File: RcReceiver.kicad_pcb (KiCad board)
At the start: 2 copper layers, 0 parts

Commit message: Add some footprints
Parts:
- added A1: E28-2G4M20S, miscellaneous:E28-2G4M20S, F.Cu at (53.0, 76.8)
- added A2: E28-2G4M20S, miscellaneous:E28-2G4M20S, F.Cu at (70.7, 76.8)
- added C1: 100nF, Capacitor_SMD:C_0402_1005Metric, F.Cu at (105.9, 83.2)
- added C10: 1uF, Capacitor_SMD:C_0402_1005Metric, F.Cu at (107.8, 82.2)
- added C11: 12pF, Capacitor_SMD:C_0402_1005Metric, F.Cu at (107.8, 83.2)
- added C12: 12pF, Capacitor_SMD:C_0402_1005Metric, F.Cu at (109.8, 83.2)
- added C13: 10uF, Capacitor_Tantalum_SMD:CP_EIA-3216-18_Kemet-A, F.Cu at (57.9, 103.3)
- added C14: 1uF, Capacitor_SMD:C_0402_1005Metric, F.Cu at (45.0, 105.9)
- added C15: 1uF, Capacitor_SMD:C_0402_1005Metric, F.Cu at (53.5, 103.8)
- added C16: 10uF, Capacitor_Tantalum_SMD:CP_EIA-3216-18_Kemet-A, F.Cu at (46.4, 104.4)
- added C17: 470pF, Capacitor_SMD:C_0402_1005Metric, F.Cu at (54.6, 105.8)
- added C18: 100nF, Capacitor_SMD:C_0402_1005Metric, F.Cu at (58.4, 104.8)
- added C19: 100nF, Capacitor_SMD:C_0402_1005Metric, F.Cu at (54.6, 104.8)
- added C2: 100nF, Capacitor_SMD:C_0402_1005Metric, F.Cu at (108.1, 81.2)
- added C20: 470pF, Capacitor_SMD:C_0402_1005Metric, F.Cu at (52.7, 105.8)
- added C21: 470pF, Capacitor_SMD:C_0402_1005Metric, F.Cu at (52.7, 104.8)
- added C22: 100nF, Capacitor_SMD:C_0402_1005Metric, F.Cu at (49.7, 103.8)
- added C23: 470pF, Capacitor_SMD:C_0402_1005Metric, F.Cu at (50.8, 105.8)
- added C24: 470pF, Capacitor_SMD:C_0402_1005Metric, F.Cu at (48.8, 105.9)
- added C25: 470pF, Capacitor_SMD:C_0402_1005Metric, F.Cu at (51.6, 103.8)
- added C26: 470pF, Capacitor_SMD:C_0402_1005Metric, F.Cu at (46.9, 105.9)
- added C27: 470pF, Capacitor_SMD:C_0402_1005Metric, F.Cu at (49.7, 104.8)
- added C28: 100nF, Capacitor_SMD:C_0402_1005Metric, F.Cu at (48.8, 91.1)
- added C29: 1uF, Capacitor_SMD:C_0402_1005Metric, F.Cu at (45.0, 91.1)
- added C3: 100nF, Capacitor_SMD:C_0402_1005Metric, F.Cu at (110.0, 81.2)
- added C30: 1uF, Capacitor_SMD:C_0402_1005Metric, F.Cu at (88.9, 63.4)
- added C31: 10uF, Capacitor_Tantalum_SMD:CP_EIA-3216-18_Kemet-A, F.Cu at (81.8, 63.9)
- added C32: 100nF, Capacitor_SMD:C_0402_1005Metric, F.Cu at (46.9, 91.1)
- added C4: 100nF, Capacitor_SMD:C_0402_1005Metric, F.Cu at (111.9, 81.2)
- added C5: 100nF, Capacitor_SMD:C_0402_1005Metric, F.Cu at (113.8, 81.2)
- added C6: 4.7uF, Capacitor_SMD:C_0402_1005Metric, F.Cu at (105.9, 82.2)
- added C7: 1uF, Capacitor_SMD:C_0402_1005Metric, F.Cu at (109.8, 82.2)
- added C8: 1uF, Capacitor_SMD:C_0402_1005Metric, F.Cu at (111.7, 82.2)
- added C9: 10nF, Capacitor_SMD:C_0402_1005Metric, F.Cu at (113.6, 82.2)
- added D1: LED, LED_SMD:LED_0402_1005Metric, F.Cu at (106.2, 81.2)
- added FB1: Ferrite_Bead, Inductor_SMD:L_0402_1005Metric, F.Cu at (131.8, 73.9)
- added J1: VBAT, Connector_PinHeader_1.27mm:PinHeader_1x02_P1.27mm_Vertical, F.Cu at (100.0, 81.9)
- added J13: CAN, Connector_JST:JST_PH_B3B-PH-SM4-TB_1x03-1MP_P2.00mm_Vertical, F.Cu at (49.8, 99.5)
- added J2: SWD, Connector_JST:JST_SH_BM05B-SRSS-TB_1x05-1MP_P1.00mm_Vertical, F.Cu at (131.5, 65.5)
- added J3: I2C, Connector_JST:JST_SH_BM05B-SRSS-TB_1x05-1MP_P1.00mm_Vertical, F.Cu at (120.7, 76.0)
- added J4: USART1, Connector_JST:JST_SH_BM04B-SRSS-TB_1x04-1MP_P1.00mm_Vertical, F.Cu at (120.2, 81.2)
- added J5: Analog input, Connector_JST:JST_SH_BM05B-SRSS-TB_1x05-1MP_P1.00mm_Vertical, F.Cu at (130.5, 70.7)
- added J6: GPS, Connector_JST:JST_SH_BM06B-SRSS-TB_1x06-1MP_P1.00mm_Vertical, F.Cu at (121.2, 70.7)
- added J7: SPI3, Connector_JST:JST_SH_BM07B-SRSS-TB_1x07-1MP_P1.00mm_Vertical, F.Cu at (121.7, 65.5)
- added R1: 2k2, Resistor_SMD:R_0402_1005Metric, F.Cu at (129.9, 74.9)
- added R2: 470k, Resistor_SMD:R_0402_1005Metric, F.Cu at (125.0, 79.1)
- added R3: 10k, Resistor_SMD:R_0402_1005Metric, F.Cu at (126.0, 77.6)
- added R4: 1k, Resistor_SMD:R_0402_1005Metric, F.Cu at (129.9, 73.9)
- added R5: 1k, Resistor_SMD:R_0402_1005Metric, F.Cu at (113.6, 83.2)
- added R6: 1k, Resistor_SMD:R_0402_1005Metric, F.Cu at (111.7, 83.2)
- added R7: 470k, Resistor_SMD:R_0402_1005Metric, F.Cu at (56.5, 106.4)
- added R8: 4k7, Resistor_SMD:R_0402_1005Metric, F.Cu at (56.5, 104.8)
- added R9: 120R, Resistor_SMD:R_0402_1005Metric, F.Cu at (61.9, 99.8)
- added U1: LP38693-3.3, miscellaneous:WSON-6_3x3mm_Pitch0.95mm, F.Cu at (127.0, 75.2)
- added U2: STM32L476VGT6, Package_QFP:LQFP-100_14x14mm_P0.5mm, F.Cu at (107.3, 71.8)
- added U3: LP38693-5.0, miscellaneous:WSON-6_3x3mm_Pitch0.95mm, F.Cu at (62.1, 104.1)
- added U4: TXB0108DQSR, Package_SON:USON-20_2x4mm_P0.4mm, F.Cu at (62.6, 97.0)
- added U5: MCP2551, digikey-footprints:SOIC-8_W3.9mm, F.Cu at (58.2, 98.5)
- added U6: LP38693SD-3.3, miscellaneous:WSON-6_3x3mm_Pitch0.95mm, F.Cu at (86.0, 64.7)
- added Y1: 16MHz, Oscillator:Oscillator_SMD_SeikoEpson_SG210-4Pin_2.5x2.0mm, F.Cu at (103.3, 82.1)

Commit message: Create PCB
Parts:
- added D2: LED_ARGB, miscellaneous:LED_Lumex-LX0404, F.Cu at (162.5, 60.0)
- added J10: Servo3, miscellaneous:PinHeader_1x03_P1.27mm_Side, F.Cu at (186.0, 52.4)
- added J11: Servo4, miscellaneous:PinHeader_1x03_P1.27mm_Side, F.Cu at (186.0, 54.9)
- added J12: Servo5, miscellaneous:PinHeader_1x03_P1.27mm_Side, F.Cu at (186.0, 57.4)
- added J14: Servo6, miscellaneous:PinHeader_1x03_P1.27mm_Side, F.Cu at (186.0, 62.5)
- added J15: Servo7, miscellaneous:PinHeader_1x03_P1.27mm_Side, F.Cu at (186.0, 65.0)
- added J16: Servo8, miscellaneous:PinHeader_1x03_P1.27mm_Side, F.Cu at (186.0, 67.6)
- added J8: Servo1, miscellaneous:PinHeader_1x03_P1.27mm_Side, F.Cu at (186.0, 47.3)
- added J9: Servo2, miscellaneous:PinHeader_1x03_P1.27mm_Side, F.Cu at (186.0, 49.8)
- A1, A2, J2, J3, J7: moved to B.Cu
- R5, R6: value 1k -> 470
- moved C24 138.3 mm to (169.5, 38.4)
- moved R7 135.0 mm to (181.6, 55.5), turned to 90 degrees
- moved C27 133.5 mm to (168.2, 43.5)
- moved C14 132.6 mm to (158.7, 37.7)
- moved C15 126.0 mm to (163.1, 41.6)
- moved U4 121.7 mm to (177.7, 57.4)
- moved C19 120.7 mm to (172.7, 79.7)
- moved A1 120.1 mm to (172.0, 60.6), turned to 180 degrees
- moved C25 120.0 mm to (170.8, 89.2)
- moved C26 119.3 mm to (165.0, 89.2)
- moved U3 118.3 mm to (179.0, 86.1)
- moved C17 112.9 mm to (164.4, 79.7)
- moved R9 111.9 mm to (172.7, 83.5)
- moved C22 110.6 mm to (159.3, 89.2)
- moved C21 109.6 mm to (159.3, 79.7)
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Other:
- board outline added: 50 x 29.5 mm

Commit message: Place all the components on the board
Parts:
- added C33: 100nF, Capacitor_SMD:C_0402_1005Metric, F.Cu at (143.8, 47.9)
- added J17: GND for the Servo connectors, Connector_PinHeader_2.54mm:PinHeader_1x01_P2.54mm_Vertical, B.Cu at (184.1, 68.9)
- added REF**: KiCad-Logo2_6mm_SilkScreen, Symbol:KiCad-Logo2_6mm_SilkScreen, F.Cu at (176.1, 72.1)
- added REF**: OSHW-Logo2_7.3x6mm_SilkScreen, Symbol:OSHW-Logo2_7.3x6mm_SilkScreen, F.Cu at (167.8, 49.6)
- C28, C32: moved to B.Cu
- J13: footprint Connector_JST:JST_PH_B3B-PH-SM4-TB_1x03-1MP_P2.00mm_Vertical -> Connector_JST:JST_SH_BM03B-SRSS-TB_1x03-1MP_P1.00mm_Vertical
- moved C7 52.4 mm to (174.3, 63.2)
- moved C32 45.4 mm to (181.6, 50.4), turned to 90 degrees
- moved R2 45.0 mm to (172.6, 66.1), turned to 90 degrees
- moved J5 43.9 mm to (139.0, 61.7), turned to 90 degrees
- moved R1 42.1 mm to (158.2, 73.5), turned to 180 degrees
- moved R6 41.4 mm to (163.1, 62.2), turned to 90 degrees
- moved J4 40.9 mm to (139.0, 50.2), turned to 90 degrees
- moved C16 40.3 mm to (175.4, 54.3)
- moved C20 40.1 mm to (181.6, 50.3), turned to 270 degrees
- moved D1 39.8 mm to (156.0, 73.5)
- moved C23 39.6 mm to (181.6, 55.4), turned to 270 degrees
- moved R5 39.5 mm to (161.9, 62.2), turned to 90 degrees
- moved C6 37.1 mm to (159.4, 51.5), turned to 90 degrees
- moved C18 36.2 mm to (174.4, 50.2), turned to 180 degrees
- moved C17 36.1 mm to (181.6, 47.9), turned to 270 degrees
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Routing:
- net Net-(C27-Pad1): track 0.00 -> 18.8 mm
- net Net-(C26-Pad1): track 0.00 -> 16.7 mm
- net Net-(C25-Pad1): track 0.00 -> 14.5 mm
- net Net-(C24-Pad1): track 0.00 -> 12.5 mm
- net Net-(C23-Pad1): track 0.00 -> 10.1 mm
- net /CANTX: track 0.00 -> 9.71 mm
- net Net-(C21-Pad1): track 0.00 -> 8.02 mm
- net Net-(C17-Pad1): track 0.00 -> 6.86 mm
- net Net-(C20-Pad1): track 0.00 -> 6.65 mm
- net Net-(J13-Pad1): track 0.00 -> 6.18 mm
- net /CANRX: track 0.00 -> 5.91 mm
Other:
- copper layers 2 -> 4
- net class Default: clearance 0.2 -> 0.1524; trace_width 0.25 -> 0.1524; via_dia 0.8 -> 0.6858; via_drill 0.4 -> 0.3302
- net class VCC added: clearance 0.1524, trace_width 0.254, via_dia 1.016, via_drill 0.635
- rule pad_to_mask_clearance: 0.051 -> 0.0508
- rule trace_clearance: 0.2 -> 0.1524
- rule trace_min: 0.2 -> 0.1524
- rule via_min_drill: 0.3 -> 0.3302
- rule via_min_size: 0.4 -> 0.6858
- board text added: "+"
- board text added: "-"
- board text added: "1019 R1"
- board text added: "An"
- board text added: "CAN"
- board text added: "GPS"
- board text added: "I2C"
- board text added: "RF Module #1"
- board text added: "RF module #2"
- board text added: "S1"
- board text added: "SPI3"
- board text added: "SWD"
- board text added: "bodri@bodrico.com"

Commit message: Start routing
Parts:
- moved C12 1.25 mm to (148.6, 48.9), turned to 90 degrees
- moved C11 0.65 mm to (153.2, 48.2), turned to 270 degrees
- moved C33 0.58 mm to (143.2, 47.9)
- moved C5 0.51 mm to (153.7, 49.7)
- moved Y1 0.37 mm to (150.9, 48.8), turned to 180 degrees
- moved C2 0.21 mm to (142.7, 66.7), turned to 180 degrees
- moved C14 0.05 mm to (172.4, 60.0)
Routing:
- net IN: track 0.00 -> 57.9 mm, vias 0 -> 2
- net /VCCCPU: track 0.00 -> 47.0 mm
- net GND: track 0.00 -> 31.9 mm
- net /GPSEN: track 0.00 -> 25.8 mm, vias 0 -> 2
- net /LEDBLUE: track 0.00 -> 25.8 mm, vias 0 -> 2
- net /LEDGREEN: track 0.00 -> 23.4 mm, vias 0 -> 2
- net /PWM2: track 0.00 -> 22.7 mm
- net /LEDRED: track 0.00 -> 19.3 mm, vias 0 -> 2
- net /GPSTX: track 0.00 -> 19.2 mm
- net /GPSRX: track 0.00 -> 18.2 mm
- net /GPSPPS: track 0.00 -> 14.2 mm
- net /Connectors/VCCOUT: track 0.00 -> 10.3 mm
- net /VBAT: track 0.00 -> 9.46 mm
- net /RF modules/VCCRF: track 0.00 -> 8.42 mm
- net Net-(J13-Pad2): track 0.00 -> 7.43 mm, vias 0 -> 2
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
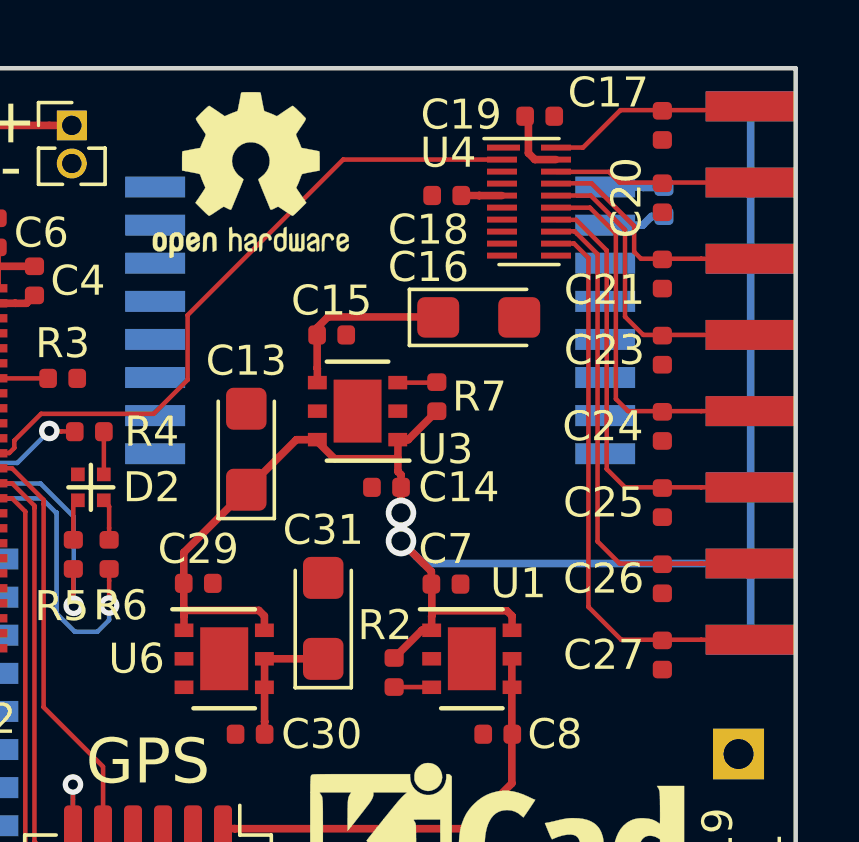
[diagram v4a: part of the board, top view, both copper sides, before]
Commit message: Fix multiple REF problem
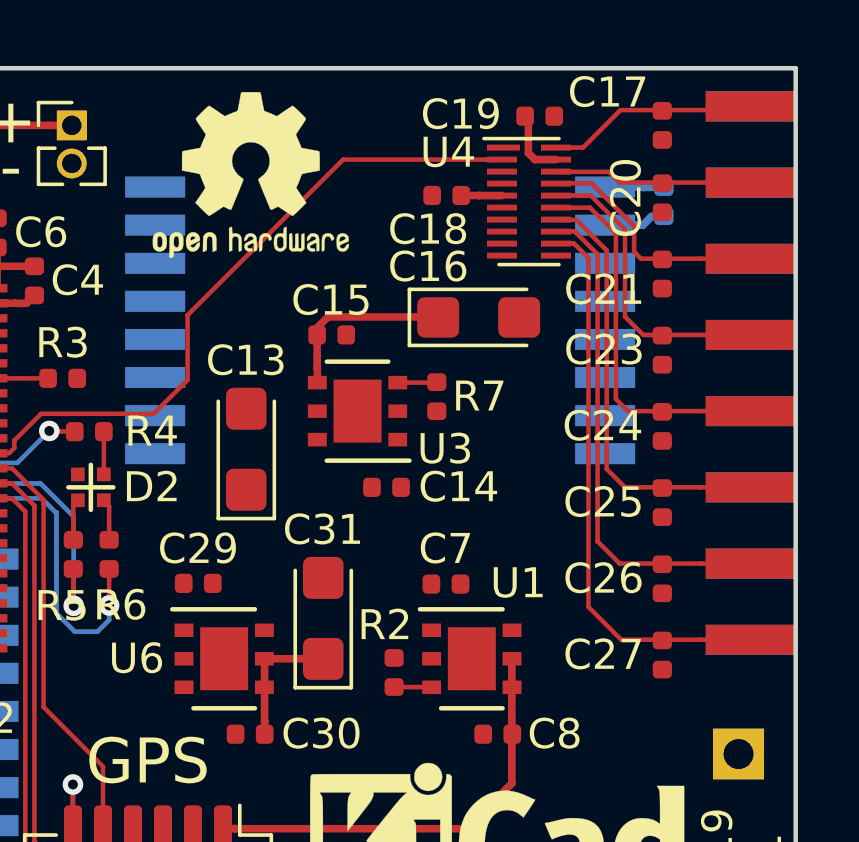
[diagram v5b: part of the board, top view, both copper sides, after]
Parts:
- renumbered REF** to KICADLOGO, REF** to OSHLOGO
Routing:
- net IN: track 57.9 -> 0.00 mm, vias 2 -> 0
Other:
- net class IN added: clearance 0.2032, trace_width 0.381, via_dia 1.016, via_drill 0.6
- net class VCC: via_drill 0.635 -> 0.6
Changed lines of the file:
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@@
     (thickness 1.6)
     (drawings 22)
-    (tracks 342)
+    (tracks 300)
     (zones 0)
     (modules 73)
@@
     (add_net "Net-(U5-Pad5)")
   )
+  (net_class IN ""
+    (clearance 0.2032)
+    (trace_width 0.381)
+    (via_dia 1.016)
+    (via_drill 0.6)
+    (uvia_dia 0.6858)
+    (uvia_drill 0.3302)
+    (diff_pair_gap 0.25)
+    (diff_pair_width 0.1524)
+    (add_net IN)
+  )
   (net_class VCC ""
     (clearance 0.1524)
     (trace_width 0.254)
     (via_dia 1.016)
-    (via_drill 0.635)
+    (via_drill 0.6)
     (uvia_dia 0.6858)
     (uvia_drill 0.3302)
@@
     (add_net /VDDA)
     (add_net GND)
-    (add_net IN)
   )
   (module Connector_JST:JST_SH_BM03B-SRSS-TB_1x03-1MP_P1.00mm_Vertical (layer F.Cu)
@@
     (tags "Logo KiCad")
     (attr virtual)
-    (fp_text reference REF** (at 0 0) (layer F.SilkS) hide
+    (fp_text reference KICADLOGO (at 0 0) (layer F.SilkS) hide
       (effects (font (size 1 1) (thickness 0.15)))
     )
@@
     (tags "Logo Symbol OSHW")
     (attr virtual)
-    (fp_text reference REF** (at 0 0) (layer F.SilkS) hide
+    (fp_text reference OSHLOGO (at 0 0) (layer F.SilkS) hide
       (effects (font (size 1 1) (thickness 0.15)))
     )
@@
   (gr_line (start 186 46) (end 186 74) (layer Edge.Cuts) (width 0.15))
   (gr_line (start 136 46) (end 186 46) (layer Edge.Cuts) (width 0.15))
-  (via (at 154.0595 74.6004) (size 0.6858) (drill 0.3302) (layers F.Cu B.Cu) (net 56))
-  (via (at 161.9081 69.876) (size 0.6858) (drill 0.3302) (layers F.Cu B.Cu) (net 56))
-  (via (at 141.55 71.908) (size 0.6858) (drill 0.3302) (layers F.Cu B.Cu) (net 63))
-  (via (at 144.471 72.67) (size 0.6858) (drill 0.3302) (layers F.Cu B.Cu) (net 63))
   (segment (start 159.979 53.835) (end 159.9799 53.8359) (width 0.254) (layer F.Cu) (net 1))
   (segment (start 158.975 53.835) (end 159.979 53.835) (width 0.254) (layer F.Cu) (net 1))
@@
   (segment (start 176.5385 68.1996) (end 176.5385 66.6375) (width 0.254) (layer F.Cu) (net 25))
   (segment (start 176.5385 66.6375) (end 176.5385 65.6723) (width 0.254) (layer F.Cu) (net 25))
-  (segment (start 158.6974 73.5082) (end 158.6974 74.7044) (width 0.254) (layer F.Cu) (net 25))
-  (segment (start 159.04241 75.04941) (end 164.90079 75.04941) (width 0.254) (layer F.Cu) (net 25))
-  (segment (start 158.6974 74.7044) (end 159.04241 75.04941) (width 0.254) (layer F.Cu) (net 25))
-  (segment (start 164.90079 75.04941) (end 166.9119 73.0383) (width 0.254) (layer F.Cu) (net 25))
-  (segment (start 166.9119 73.0383) (end 166.9119 71.3492) (width 0.254) (layer F.Cu) (net 25))
   (segment (start 158.6974 73.0882) (end 157.3742 71.765) (width 0.254) (layer F.Cu) (net 25))
   (segment (start 158.6974 73.5082) (end 158.6974 73.0882) (width 0.254) (layer F.Cu) (net 25))
@@
   (segment (start 143.1653 66.7264) (end 143.1653 65.3397) (width 0.254) (layer F.Cu) (net 25))
   (segment (start 143.1653 65.3397) (end 143.1756 65.3294) (width 0.254) (layer F.Cu) (net 25))
-  (segment (start 172.6142 65.6572) (end 173.5389 64.7325) (width 0.254) (layer F.Cu) (net 26))
-  (segment (start 173.5389 64.7325) (end 173.8715 64.7325) (width 0.254) (layer F.Cu) (net 26))
-  (segment (start 173.865 64.256) (end 173.8715 64.2495) (width 0.254) (layer F.Cu) (net 26))
-  (segment (start 173.865 64.735) (end 173.865 64.256) (width 0.254) (layer F.Cu) (net 26))
-  (segment (start 172.8452 59.55) (end 172.7412 59.446) (width 0.254) (layer F.Cu) (net 26))
-  (segment (start 172.8452 59.97) (end 172.8452 59.55) (width 0.254) (layer F.Cu) (net 26))
-  (segment (start 172.7412 58.3825) (end 173.0841 58.3825) (width 0.254) (layer F.Cu) (net 26))
-  (segment (start 173.0841 58.3825) (end 174.0366 57.43) (width 0.254) (layer F.Cu) (net 26))
-  (segment (start 170.629578 59.0175) (end 172.7412 59.0175) (width 0.254) (layer F.Cu) (net 26))
-  (segment (start 170.055 58.442922) (end 170.629578 59.0175) (width 0.254) (layer F.Cu) (net 26))
-  (segment (start 170.055 58.38) (end 170.055 58.442922) (width 0.254) (layer F.Cu) (net 26))
-  (segment (start 172.7412 59.446) (end 172.7412 59.0175) (width 0.254) (layer F.Cu) (net 26))
-  (segment (start 172.7412 59.0175) (end 172.7412 58.3825) (width 0.254) (layer F.Cu) (net 26))
-  (segment (start 167.6866 60.05) (end 169.3541 58.3825) (width 0.254) (layer F.Cu) (net 26))
-  (segment (start 169.3541 58.3825) (end 170.0361 58.3825) (width 0.254) (layer F.Cu) (net 26))
-  (segment (start 173.8564 62.7758) (end 172.8428 61.7622) (width 0.254) (layer F.Cu) (net 26))
-  (segment (start 173.8564 63.1958) (end 173.8564 62.7758) (width 0.254) (layer F.Cu) (net 26))
-  (segment (start 176.3738 64.0848) (end 173.8715 64.0848) (width 0.254) (layer F.Cu) (net 26))
-  (segment (start 176.545 64.256) (end 176.3738 64.0848) (width 0.254) (layer F.Cu) (net 26))
-  (segment (start 176.545 64.735) (end 176.545 64.256) (width 0.254) (layer F.Cu) (net 26))
-  (segment (start 173.8715 64.2495) (end 173.8715 64.0848) (width 0.254) (layer F.Cu) (net 26))
-  (segment (start 173.8715 64.0848) (end 173.8715 63.1958) (width 0.254) (layer F.Cu) (net 26))
-  (segment (start 165.61 64.256) (end 165.6038 64.2498) (width 0.254) (layer F.Cu) (net 26))
-  (segment (start 165.61 64.735) (end 165.61 64.256) (width 0.254) (layer F.Cu) (net 26))
-  (segment (start 165.6038 63.1704) (end 165.6038 62.1417) (width 0.254) (layer F.Cu) (net 26))
-  (segment (start 165.6038 62.1417) (end 167.6866 60.0589) (width 0.254) (layer F.Cu) (net 26))
-  (segment (start 168.1061 64.0721) (end 165.6038 64.0721) (width 0.254) (layer F.Cu) (net 26))
-  (segment (start 168.29 64.256) (end 168.1061 64.0721) (width 0.254) (layer F.Cu) (net 26))
-  (segment (start 168.29 64.735) (end 168.29 64.256) (width 0.254) (layer F.Cu) (net 26))
-  (segment (start 165.6038 64.2498) (end 165.6038 64.0721) (width 0.254) (layer F.Cu) (net 26))
-  (segment (start 165.6038 64.0721) (end 165.6038 63.1704) (width 0.254) (layer F.Cu) (net 26))
-  (segment (start 172.8428 61.7622) (end 172.8428 61.7622) (width 0.254) (layer F.Cu) (net 26))
-  (via (at 172.8428 61.7622) (size 1.016) (drill 0.635) (layers F.Cu B.Cu) (net 26))
-  (segment (start 173.350799 62.270199) (end 173.352299 62.270199) (width 0.254) (layer B.Cu) (net 26))
-  (segment (start 172.8428 61.7622) (end 173.350799 62.270199) (width 0.254) (layer B.Cu) (net 26))
-  (segment (start 173.352299 62.270199) (end 173.5921 62.51) (width 0.254) (layer B.Cu) (net 26))
-  (segment (start 173.5921 62.51) (end 184.5014 62.51) (width 0.254) (layer B.Cu) (net 26))
-  (segment (start 184.5 65.05) (end 184.5 47.2813) (width 0.254) (layer B.Cu) (net 26))
-  (segment (start 184.5 47.2813) (end 184.4887 47.27) (width 0.254) (layer B.Cu) (net 26))
-  (segment (start 172.8428 60.8209) (end 172.8428 59.97) (width 0.254) (layer F.Cu) (net 26))
-  (via (at 172.8428 60.8209) (size 1.016) (drill 0.635) (layers F.Cu B.Cu) (net 26))
-  (segment (start 172.8428 61.7622) (end 172.8428 60.8209) (width 0.254) (layer B.Cu) (net 26))
+  (segment (start 158.6974 73.5082) (end 158.6974 74.7044) (width 0.254) (layer F.Cu) (net 25) (status 1000000))
+  (segment (start 164.90079 75.04941) (end 166.9119 73.0383) (width 0.254) (layer F.Cu) (net 25) (status 1000000))
+  (segment (start 159.04241 75.04941) (end 164.90079 75.04941) (width 0.254) (layer F.Cu) (net 25) (status 1000000))
+  (segment (start 158.6974 74.7044) (end 159.04241 75.04941) (width 0.254) (layer F.Cu) (net 25) (status 1000000))
+  (segment (start 166.9119 73.0383) (end 166.9119 71.3492) (width 0.254) (layer F.Cu) (net 25) (status 1000000))
   (segment (start 146.575 50.431) (end 146.5919 50.4141) (width 0.254) (layer F.Cu) (net 27))
   (segment (start 146.575 51.435) (end 146.575 50.431) (width 0.254) (layer F.Cu) (net 27))
@@
   (segment (start 160.93022 67.29792) (end 162.9114 69.2791) (width 0.1524) (layer F.Cu) (net 55))
   (segment (start 162.9114 69.2791) (end 162.9114 71.3365) (width 0.1524) (layer F.Cu) (net 55))
+  (via (at 154.0595 74.6004) (size 0.6858) (drill 0.3302) (layers F.Cu B.Cu) (net 56))
+  (via (at 161.9081 69.876) (size 0.6858) (drill 0.3302) (layers F.Cu B.Cu) (net 56))
   (segment (start 161.9081 69.876) (end 161.9081 70.360933) (width 0.1524) (layer F.Cu) (net 56))
   (segment (start 161.9081 70.360933) (end 161.9081 71.3492) (width 0.1524) (layer F.Cu) (net 56))
@@
   (segment (start 142.7438 71.4) (end 141.7278 72.416) (width 0.1524) (layer F.Cu) (net 62))
   (segment (start 141.7278 72.416) (end 140.3308 72.416) (width 0.1524) (layer F.Cu) (net 62))
+  (via (at 141.55 71.908) (size 0.6858) (drill 0.3302) (layers F.Cu B.Cu) (net 63))
+  (via (at 144.471 72.67) (size 0.6858) (drill 0.3302) (layers F.Cu B.Cu) (net 63))
   (segment (start 144.471 72.67) (end 146.0966 72.67) (width 0.1524) (layer F.Cu) (net 63))
   (segment (start 144.471 72.67) (end 143.986067 72.67) (width 0.1524) (layer F.Cu) (net 63))
